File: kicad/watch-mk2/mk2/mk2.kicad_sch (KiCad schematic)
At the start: 71 parts, among them IC1 113990582, IC2 M41T62LC6F, J1 FPC24-0.5mm, J2 USB_C_Receptacle_USB2.0, J3 Conn_01x02_Female, Q1 Si1308EDL, Q2 Si1308EDL, Q3 Si1308EDL, Q4 Si1308EDL, SW1 B5, SW2 B1, SW3 B2, SW4 B3, SW5 B4, U1 W25X20CLUXIG, U2 LM3671MF-2.8_NOPB, U3 MCP73831-2-OT, Y1 32.768kHz

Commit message: add rev2mk2
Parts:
- removed C10, C11, C12, C13, C14, C15, C16, C17, C18, C19, C9: 1uF, Capacitor_SMD:C_0603_1608Metric_Pad1.05x0.95mm_HandSolder, symbol Device:C_Small
- removed C8: 4.7uF, Capacitor_SMD:C_0603_1608Metric_Pad1.05x0.95mm_HandSolder, symbol Device:C_Small
- removed D3, D4, D5: MBR0530, Diode_SMD:D_SOD-123, symbol Device:D_Schottky
- removed D6: CHRG_LED, LED_SMD:LED_0603_1608Metric_Pad1.05x0.95mm_HandSolder, symbol Device:LED
- removed D7: FLASHLIGHT, Connector_PinHeader_2.54mm:PinHeader_1x02_P2.54mm_Vertical, symbol Device:LED
- removed D8: BACKLIGHT, Connector_PinHeader_2.54mm:PinHeader_1x02_P2.54mm_Vertical, symbol Device:LED
- removed J1: FPC24-0.5mm, Connector_FFC-FPC:Hirose_FH12-24S-0.5SH_1x24-1MP_P0.50mm_Horizontal, symbol Connector:Conn_01x24_Female
- removed Q1, Q2: Si1308EDL, Package_TO_SOT_SMD:SOT-323_SC-70, symbol Device:Q_NMOS_GSD
- removed R1, R2: 1k, Resistor_SMD:R_0603_1608Metric_Pad1.05x0.95mm_HandSolder, symbol Device:R
- removed R10: 470, Resistor_SMD:R_0603_1608Metric_Pad1.05x0.95mm_HandSolder, symbol Device:R
- removed R7: 10k, Resistor_SMD:R_0603_1608Metric_Pad1.05x0.95mm_HandSolder, symbol Device:R
- removed R8: 3, Resistor_SMD:R_0603_1608Metric_Pad1.05x0.95mm_HandSolder, symbol Device:R
- removed SW3: B2, libs:E-Switch-TL3330AF130QG-MFG, symbol Switch:SW_Push
- removed SW5: B4, libs:E-Switch-TL3330AF130QG-MFG, symbol Switch:SW_Push
- removed SW_BOOT1: SW_Push, Button_Switch_SMD:SW_SPST_CK_KXT3, symbol Switch:SW_Push
- added C10: 0.47uF, Capacitor_SMD:C_0603_1608Metric_Pad1.05x0.95mm_HandSolder, symbol Device:C
- added C8: 10uF, Capacitor_SMD:C_0603_1608Metric_Pad1.05x0.95mm_HandSolder, symbol Device:C
- added C9: 560pF, Capacitor_SMD:C_0603_1608Metric_Pad1.05x0.95mm_HandSolder, symbol Device:C
- added J1: Conn_01x10_Female, Connector_FFC-FPC:Hirose_FH12-10S-0.5SH_1x10-1MP_P0.50mm_Horizontal, symbol Connector:Conn_01x10_Female
- added J5: Conn_01x04_Female, libs:ffc-0.5mm-4, symbol Connector:Conn_01x04_Female
- added JP1: FUEL_BYP, Resistor_SMD:R_0603_1608Metric, symbol Device:Jumper_NO_Small
- added P1: AXT610124, libs:PANASONIC_AXT610124, symbol AXT610124:AXT610124
- added U5: MAX17220ELT+, max17220:Maxim_Integrated-L622-1C-0-E-IPC_A, symbol max17220:MAX17220ELT+
- added U6: MAX17262REWL+T, max17262:Maxim-W91G1-3-0-A-IPC_A, symbol max17262:MAX17262REWL+T
- BT1: footprint Connector_JST:JST_PH_B2B-PH-K_1x02_P2.00mm_Vertical -> Connector_JST:JST_SH_BM02B-SRSS-TB_1x02-1MP_P1.00mm_Vertical; package (none) -> DNP
- C1, C2: LCSC (none) -> C38523; package (none) -> 0603
- C20, C4: LCSC (none) -> C19666; package (none) -> 0603
- C3, C7: LCSC (none) -> C19702; package (none) -> 0603
- C5, D2, IC2, J2, J3, SW1, SW2, SW4, SW_RESET1, TP1, TP2, TP3, TP4, U2, Y1: package (none) -> DNP
- C6: value 4.7uF -> 10uF; LCSC (none) -> C19702; package (none) -> 0603
- D1: LCSC (none) -> C155330; package (none) -> DNP
- IC1: value 113990582 -> MDBT50Q; package (none) -> DNP
- L1: package (none) -> 0603
- L2: value 10uH -> 2.2uH; package (none) -> 0603
- Q3, Q4: LCSC (none) -> C469327; package (none) -> DNP
- R11, R12: LCSC (none) -> C23186; package (none) -> 0603
- R13, R15: value 1k -> 100k; LCSC (none) -> C25803; package (none) -> 0603
- R14, R16: LCSC (none) -> C21190; package (none) -> 0603
- R3, R4: LCSC (none) -> C25190; package (none) -> 0603
- R5: value 10k -> 100k; LCSC (none) -> C25803; package (none) -> 0603
- R6: LCSC (none) -> C25804; package (none) -> 0603
- R9: LCSC (none) -> C22975; package (none) -> 0603
- U1: footprint Package_SO:TSSOP-8_4.4x3mm_P0.65mm -> libs:SON50P300X200X60-9N; LCSC (none) -> C164121; package (none) -> DNP
- U3: LCSC (none) -> C14879; package (none) -> DNP
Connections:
- net EPBUSY is gone; now on net BUTTON4: IC1.48 (P0.24)
- net EPDC is gone; now on net SCL: IC1.46 (P0.22)
- net EPSCLK is gone; now on net SDA: IC1.44 (P0.20)
- net +BATT: now also JP1.1, U6.A1 (TH), U6.A2 (BATT); no longer C20.1, D1.1 (A), U3.3 (VBAT)
- net BUTTON1: now also IC1.22 (P0.06); no longer IC1.10 (P0.29)
- net BUTTON2: now also IC1.50 (P1.02), P1.5; no longer IC1.8 (P1.15)
- net BUTTON3: now also IC1.26 (P1.09); no longer IC1.52 (P0.09/NFC1)
- net BUTTON4: now also P1.7; no longer IC1.54 (P0.10/NFC2)
- net BUTTON5: now also IC1.24 (P0.08); no longer IC1.12 (P0.31)
- net BUZZER: now also IC1.13 (P0.28); no longer IC1.6 (P1.13)
- net FLASHLIGHT: now also IC1.49 (P0.25), P1.3; no longer IC1.36 (P0.14)
- net FLASH_CS: now also IC1.16 (P0.27); no longer IC1.20 (P0.04)
- net GND: now also C6.2, TP1.1, C10.2, C8.2, C9.2, J1.10 (Pin_10), J1.9 (Pin_9), P1.9, U5.3 (GND), U5.4 (SEL), U6.C3 (GND); no longer C6.1, TP4.1
- net RTCIRQ: now also IC1.41 (P0.17); no longer IC1.14 (P0.30)
- net SCL: now also U6.B1 (SCL); no longer IC1.16 (P0.27)
- net SDA: now also U6.C1 (SDA); no longer IC1.19 (P0.26)
- net SQW: now also IC1.42 (P0.19), J1.4 (Pin_4); no longer IC1.13 (P0.28)
- net SWDIO: now also TP4.1; no longer TP1.1
- net VCC: now also R5.2, P1.2; no longer C6.2, L2.1, R5.1
- net VIN: now also C6.1, L2.1, P1.1, U5.5 (IN), U5.6 (EN)
- net VUSB: now also D1.1 (A); no longer D1.2 (A)
- net at Q3.3 (D): now also J5.3 (Pin_3), J5.4 (Pin_4)
- net at R14.2: now also J5.1 (Pin_1), J5.2 (Pin_2)
- net CHGNG: now reaches U3.1 (STAT)
- net CHGNG: now also IC1.52 (P0.09/NFC1), R5.1
- net at L2.2: now also U5.2 (LX)
- net BOOTLOAD renamed LCD_CS
- net LCD_CS: now also J1.3 (Pin_3); no longer R5.2
- net EPCS: no longer names the net of IC1.45 (P0.23)
- net EPRES: no longer names the net of IC1.47 (P1.00)
- net EPSDIN: no longer names the net of IC1.43 (P0.21)
- net FLASH_CLK renamed SPI_CLK
- net SPI_CLK: now also IC1.10 (P0.29), J1.1 (Pin_1); no longer IC1.24 (P0.08)
- net FLASH_DI renamed SPI_MOSI
- net SPI_MOSI: now also IC1.12 (P0.31), J1.2 (Pin_2); no longer IC1.26 (P1.09)
- net FLASH_DO renamed SPI_MISO
- net SPI_MISO: now also IC1.14 (P0.30); no longer IC1.22 (P0.06)
- new net: C10.1, U6.C2 (REG)
- new net 5V: C8.1, J1.6 (Pin_6), J1.7 (Pin_7), J1.8 (Pin_8), U5.1 (OUT)
- new net BATTIRQ: IC1.54 (P0.10/NFC2)
- new net BATTPOW: C20.1, D1.2 (A), JP1.2, U3.3 (VBAT), U6.B3 (SYS)
- new net LCD_DISP: C9.1, J1.5 (Pin_5)
- no-connect marks 28 -> 35
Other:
- note added: "IRQ needs pullup"
- note added: "need shunt diode to prevent cap from overcharging (??)"
- note removed: "based on https://www.waveshare.com/w/upload/8/80/E-Paper_ESP32_Driver_Board_Schematic.pdf"
- moved on the sheet: D2

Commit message: commit rev3
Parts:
- removed C5: 11mF, Capacitor_SMD:C_1210_3225Metric_Pad1.42x2.65mm_HandSolder, symbol Device:C
- removed C6: 10uF, Capacitor_SMD:C_0603_1608Metric_Pad1.05x0.95mm_HandSolder, symbol Device:C_Small
- removed C8: 10uF, Capacitor_SMD:C_0603_1608Metric_Pad1.05x0.95mm_HandSolder, symbol Device:C
- removed D2: D_Schottky, Diode_SMD:D_0603_1608Metric_Pad1.05x0.95mm_HandSolder, symbol Device:D_Schottky
- removed J5: Conn_01x04_Female, libs:ffc-0.5mm-4, symbol Connector:Conn_01x04_Female
- removed JP1: FUEL_BYP, Resistor_SMD:R_0603_1608Metric, symbol Device:Jumper_NO_Small
- removed L2: 2.2uH, Inductor_SMD:L_0603_1608Metric_Pad1.05x0.95mm_HandSolder, symbol Device:L
- removed R5: 100k, Resistor_SMD:R_0603_1608Metric_Pad1.05x0.95mm_HandSolder, symbol Device:R
- removed U1: W25X20CLUXIG, libs:SON50P300X200X60-9N, symbol Memory_Flash:AT25SF081-XMHF-X
- removed U5: MAX17220ELT+, max17220:Maxim_Integrated-L622-1C-0-E-IPC_A, symbol max17220:MAX17220ELT+
- added J4: 503480-0400, libs:MOLEX_503480-0400, symbol molex_503480-0400:503480-0400
- added U4: BMA400, libs:XDCR_BMA400, symbol BMA400:BMA400
- BT1: footprint Connector_JST:JST_SH_BM02B-SRSS-TB_1x02-1MP_P1.00mm_Vertical -> Connector_PinHeader_2.00mm:PinHeader_1x02_P2.00mm_Vertical
- J3: footprint Connector_PinHeader_1.00mm:PinHeader_1x02_P1.00mm_Vertical -> Connector_PinHeader_2.00mm:PinHeader_1x02_P2.00mm_Vertical
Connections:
- net 5V is gone; now on net VIN: J1.6 (Pin_6), J1.7 (Pin_7), J1.8 (Pin_8)
- net BACKLIGHT: now also IC1.45 (P0.23); no longer IC1.21 (P0.05)
- net GND: now also U4.1 (SDO), U4.8 (GNDIO), U4.9 (GND)
- net SCL: now also U4.12 (SCX)
- net SDA: now also U4.2 (SDX)
- net VCC: now also IC2.5 (VCC), U4.10 (~CSB~), U4.3 (VDDIO), U4.7 (VDD)
- net at R14.2: now also J4.1, J4.2
- net ACCELINT1: now reaches IC1.7 (P1.14)
- net ACCELINT1: now also U4.5 (INT1)
- net ACCELINT2: now reaches IC1.9 (P0.03)
- net ACCELINT2: now also U4.6 (INT2)
- net at Q3.3 (D): now also J4.3, J4.4
- net FLASH_CS: no longer names the net of IC1.16 (P0.27)
- no-connect marks 35 -> 36
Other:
- note removed: "IRQ needs pullup"
- note removed: "need shunt diode to prevent cap from overcharging (??)"
- moved on the sheet: J3, Q4, R15, R16

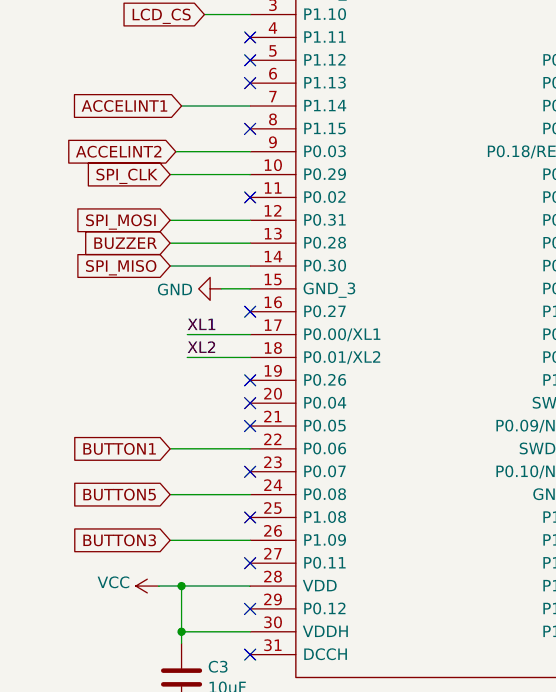
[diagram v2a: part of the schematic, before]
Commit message: add rev2 of flex cable
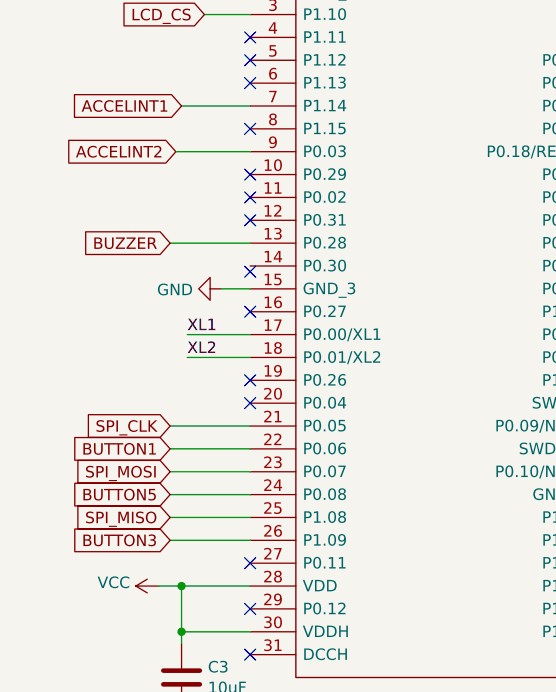
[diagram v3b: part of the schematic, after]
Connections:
- net SPI_CLK: now also IC1.21 (P0.05); no longer IC1.10 (P0.29)
- net SPI_MISO: now also IC1.25 (P1.08); no longer IC1.14 (P0.30)
- net SPI_MOSI: now also IC1.23 (P0.07); no longer IC1.12 (P0.31)
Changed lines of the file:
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@@
   (junction (at 254 147.955) (diameter 0) (color 0 0 0 0))
   (junction (at 254 155.575) (diameter 0) (color 0 0 0 0))
+  (no_connect (at 145.415 130.175))
+  (no_connect (at 38.735 144.78))
+  (no_connect (at 177.8 208.28))
+  (no_connect (at 145.415 132.715))
+  (no_connect (at 38.735 154.94))
+  (no_connect (at 38.735 132.08))
+  (no_connect (at 128.27 212.09))
+  (no_connect (at 177.8 205.74))
+  (no_connect (at 38.735 152.4))
+  (no_connect (at 125.73 212.09))
+  (no_connect (at 81.915 172.72))
+  (no_connect (at 81.915 170.18))
+  (no_connect (at 240.03 102.235))
+  (no_connect (at 81.915 144.78))
+  (no_connect (at 38.735 172.72))
+  (no_connect (at 38.735 129.54))
+  (no_connect (at 38.735 134.62))
+  (no_connect (at 38.735 140.335))
+  (no_connect (at 38.735 116.84))
+  (no_connect (at 81.915 175.26))
+  (no_connect (at 81.915 134.62))
+  (no_connect (at 81.915 124.46))
+  (no_connect (at 133.35 212.09))
+  (no_connect (at 240.03 84.455))
+  (no_connect (at 81.915 180.34))
+  (no_connect (at 81.915 121.92))
+  (no_connect (at 130.81 212.09))
+  (no_connect (at 81.915 167.64))
   (no_connect (at 81.915 116.84))
-  (no_connect (at 81.915 172.72))
-  (no_connect (at 125.73 212.09))
-  (no_connect (at 38.735 157.48))
-  (no_connect (at 38.735 162.56))
-  (no_connect (at 38.735 124.46))
-  (no_connect (at 177.8 205.74))
-  (no_connect (at 177.8 208.28))
-  (no_connect (at 81.915 134.62))
-  (no_connect (at 38.735 172.72))
-  (no_connect (at 81.915 175.26))
-  (no_connect (at 240.03 84.455))
-  (no_connect (at 38.735 154.94))
-  (no_connect (at 128.27 212.09))
-  (no_connect (at 81.915 167.64))
+  (no_connect (at 81.915 177.8))
   (no_connect (at 38.735 119.38))
-  (no_connect (at 38.735 167.64))
-  (no_connect (at 240.03 102.235))
-  (no_connect (at 38.735 132.08))
-  (no_connect (at 81.915 170.18))
-  (no_connect (at 133.35 212.09))
-  (no_connect (at 81.915 180.34))
-  (no_connect (at 81.915 124.46))
-  (no_connect (at 81.915 121.92))
-  (no_connect (at 38.735 116.84))
-  (no_connect (at 38.735 152.4))
   (no_connect (at 38.735 177.8))
-  (no_connect (at 130.81 212.09))
+  (no_connect (at 38.735 182.88))
   (no_connect (at 38.735 114.3))
   (no_connect (at 81.915 119.38))
-  (no_connect (at 81.915 177.8))
-  (no_connect (at 145.415 130.175))
-  (no_connect (at 38.735 182.88))
-  (no_connect (at 81.915 144.78))
-  (no_connect (at 145.415 132.715))
-  (no_connect (at 38.735 144.78))
+  (no_connect (at 38.735 124.46))
   (wire (pts (xy 15.24 85.09) (xy 17.78 85.09))
     (stroke (width 0) (type solid) (color 0 0 0 0))
@@
     (stroke (width 0) (type solid) (color 0 0 0 0))
   )
-  (wire (pts (xy 29.845 129.54) (xy 38.735 129.54))
-    (stroke (width 0) (type solid) (color 0 0 0 0))
-  )
-  (wire (pts (xy 29.845 134.62) (xy 38.735 134.62))
-    (stroke (width 0) (type solid) (color 0 0 0 0))
-  )
   (wire (pts (xy 29.845 137.16) (xy 38.735 137.16))
     (stroke (width 0) (type solid) (color 0 0 0 0))
   )
-  (wire (pts (xy 29.845 139.7) (xy 38.735 139.7))
+  (wire (pts (xy 29.845 157.48) (xy 38.735 157.48))
     (stroke (width 0) (type solid) (color 0 0 0 0))
   )
@@
     (stroke (width 0) (type solid) (color 0 0 0 0))
   )
+  (wire (pts (xy 29.845 162.56) (xy 38.735 162.56))
+    (stroke (width 0) (type solid) (color 0 0 0 0))
+  )
   (wire (pts (xy 29.845 165.1) (xy 38.735 165.1))
+    (stroke (width 0) (type solid) (color 0 0 0 0))
+  )
+  (wire (pts (xy 29.845 167.64) (xy 38.735 167.64))
     (stroke (width 0) (type solid) (color 0 0 0 0))
   )
@@
     (effects (font (size 1.27 1.27)) (justify left bottom))
   )
-  (global_label "SPI_CLK" (shape input) (at 29.845 129.54 180)
-    (effects (font (size 1.27 1.27)) (justify right))
-  )
-  (global_label "SPI_MOSI" (shape input) (at 29.845 134.62 180)
-    (effects (font (size 1.27 1.27)) (justify right))
-  )
   (global_label "BUZZER" (shape input) (at 29.845 137.16 180)
     (effects (font (size 1.27 1.27)) (justify right))
   )
-  (global_label "SPI_MISO" (shape input) (at 29.845 139.7 180)
+  (global_label "SPI_CLK" (shape input) (at 29.845 157.48 180)
     (effects (font (size 1.27 1.27)) (justify right))
   )
@@
     (effects (font (size 1.27 1.27)) (justify right))
   )
+  (global_label "SPI_MOSI" (shape input) (at 29.845 162.56 180)
+    (effects (font (size 1.27 1.27)) (justify right))
+  )
   (global_label "BUTTON5" (shape input) (at 29.845 165.1 180)
     (effects (font (size 1.27 1.27)) (justify right))
   )
+  (global_label "SPI_MISO" (shape input) (at 29.845 167.64 180)
+    (effects (font (size 1.27 1.27)) (justify right))
+  )

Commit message: schematic checkpoint
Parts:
- added C5, C6, C8: 2.2uF, Capacitor_SMD:C_0603_1608Metric_Pad1.05x0.95mm_HandSolder, symbol Device:C
- added J5, J6: Conn_01x02_Female, Connector_PinHeader_2.00mm:PinHeader_1x02_P2.00mm_Vertical, symbol Connector:Conn_01x02_Female
- added TP5, TP6: TestPoint, TestPoint:TestPoint_Pad_D1.0mm, symbol Connector:TestPoint
- added U1: TPS60151DRV, Package_SON:WSON-6-1EP_2x2mm_P0.65mm_EP1x1.6mm_ThermalVias, symbol Regulator_SwitchedCapacitor:TPS60151DRV
- R14: value 1k -> 100
- R16: value 1k -> 10
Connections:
- net GND: now also C5.1, C8.2, J5.2 (Pin_2), U1.1 (GND), U1.7 (EP)
- net LCD_DISP: now also IC1.4 (P1.11)
- net USB_DN: now also J6.1 (Pin_1)
- net USB_DP: now also J6.2 (Pin_2)
- net VIN: now also C5.2, TP5.1, U1.2 (VIN), U1.6 (ENA); no longer J1.6 (Pin_6), J1.7 (Pin_7), J1.8 (Pin_8)
- net VUSB: now also J5.1 (Pin_1)
- new net: C6.1, U1.4 (CP+)
- new net: C6.2, U1.5 (CP-)
- new net +5V: C8.1, J1.6 (Pin_6), J1.7 (Pin_7), J1.8 (Pin_8), TP6.1, U1.3 (VOUT)
- no-connect marks 36 -> 35
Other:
- moved on the sheet: D1

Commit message: checkpoint
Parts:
- removed J2: USB_C_Receptacle_USB2.0, Connector_USB:USB_C_Receptacle_Palconn_UTC16-G, symbol Connector:USB_C_Receptacle_USB2.0
- removed J5: Conn_01x02_Female, Connector_PinHeader_2.00mm:PinHeader_1x02_P2.00mm_Vertical, symbol Connector:Conn_01x02_Female
- removed P1: AXT610124, libs:PANASONIC_AXT610124, symbol AXT610124:AXT610124
- removed R6: 10k, Resistor_SMD:R_0603_1608Metric_Pad1.05x0.95mm_HandSolder, symbol Device:R
- removed SW_RESET1: SW_Push, Button_Switch_SMD:SW_SPST_CK_KXT3, symbol Switch:SW_Push
- added D2: D_Schottky_x2_KCom_AAK, Package_TO_SOT_SMD:TSOT-23, symbol Device:D_Schottky_x2_KCom_AAK
- added J2: 2305018-2, te-waterproof-usb-2305018-2:TE_2305018-2, symbol 2305018-2:2305018-2
- added JP1, JP2: Jumper_NO_Small, Jumper:SolderJumper-2_P1.3mm_Open_Pad1.0x1.5mm, symbol Device:Jumper_NO_Small
- added JP3: Jumper_NC_Small, Jumper:SolderJumper-2_P1.3mm_Bridged_Pad1.0x1.5mm, symbol Device:Jumper_NC_Small
- added Q1: Si1308EDL, Package_TO_SOT_SMD:SOT-323_SC-70, symbol Device:Q_NMOS_GSD
- added R1: shunt, Resistor_SMD:R_0603_1608Metric, symbol Device:R
- added R2: 100k, Resistor_SMD:R_0603_1608Metric_Pad1.05x0.95mm_HandSolder, symbol Device:R
- added U5: TPD2S017, Package_TO_SOT_SMD:SOT-23-6, symbol Power_Protection:TPD2S017
- J6: footprint Connector_PinHeader_2.00mm:PinHeader_1x02_P2.00mm_Vertical -> Connector_PinSocket_2.00mm:PinSocket_1x02_P2.00mm_Vertical; package (none) -> DNP
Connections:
- net +5V: now also D2.2 (A), JP1.2; no longer J1.6 (Pin_6), J1.7 (Pin_7), J1.8 (Pin_8)
- net FLASHLIGHT: now also Q1.1 (G), R2.1
- net GND: now also R12.1, J2.A1 (GNDA), J2.A12 (GNDA__1), J2.B1 (GNDB), J2.B12 (GNDB__1), J2.G1 (GND), J2.G2 (GND__1), J2.S1 (SHIELD), J2.S2 (SHIELD__1), J2.S3 (SHIELD__2), J2.S4 (SHIELD__3), JP2.2, Q1.2 (S), R2.2, U5.2 (GND); no longer R12.2
- net RST: now also JP2.1
- net USB_DN: now also U5.1 (CH1Out); no longer J6.1 (Pin_1)
- net USB_DP: now also U5.6 (CH2Out); no longer J6.2 (Pin_2)
- net VIN: now also J6.1 (Pin_1), D2.1 (A), JP3.1, R1.2; no longer D1.3 (K), U1.6 (ENA)
- net VUSB: now also J2.A4 (VBUS_A), J2.A9 (VBUS_A__1), J2.B4 (VBUS_B), J2.B9 (VBUS_B__1), U5.5 (VCC)
- net 5VREG_EN: now reaches IC1.16 (P0.27)
- net 5VREG_EN: now also U1.6 (ENA)
- net SPARE: now reaches IC1.37 (P0.13)
- net SIDE_INT: now reaches IC1.43 (P0.21)
- net at R11.1: now also J2.B5 (CC2)
- net BUTTON2: no longer names the net of IC1.50 (P1.02)
- net BUTTON4: no longer names the net of IC1.48 (P0.24)
- new net: J2.A5 (CC1), R12.2
- new net: D1.3 (K), JP3.2, R1.1
- new net: J6.2 (Pin_2), Q1.3 (D)
- new net DISP_POWER: D2.3 (K), J1.6 (Pin_6), J1.7 (Pin_7), J1.8 (Pin_8), JP1.1
- new net USB_DN_EXT: J2.A7 (DA_N), J2.B7 (DB_N), U5.3 (CH1In)
- new net USB_DP_EXT: J2.A6 (DA_P), J2.B6 (DB_P), U5.4 (CH2Int)
- no-connect marks 35 -> 38
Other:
- note added: "2k -> 500mA charge current (1C) 5.1k -> ~~200mA"
- note added: "RST pulled up internally"
- note removed: "2k -> 500mA charge current (1C)"
- moved on the sheet: C1, C2, C3, C5, D1, IC1, IC2, R11, R12, R3, R4, U4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

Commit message: checkpoint
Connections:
- net BATTPOW: no longer D1.2 (A)
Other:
- note added: "2k -> 500mA charge current (1C) 5.1k -> ~200mA"
- note added: "Display and Backlight"
- note added: "I/O"
- note added: "Jeff Cooper - jeff@thejeffcooper.com - Pittsburgh, PA"
- note added: "NOTE: Unclear if this 5V regulator is actually effective at such a low current level"
- note added: "Peripherals"
- note added: "Power and Battery"
- note added: "RTC"
- note added: "Sharp Memory LCD"
- note added: "Test Points"
- note added: "USB"
- note added: "accelerometer"
- note added: "https://hackaday.io/project/169967-nrf52-smartwatch"
- note added: "nRF52840"
- note added: "nRF52840 Smartwatch"
- note removed: "2k -> 500mA charge current (1C) 5.1k -> ~~200mA"
- moved on the sheet: BT1, C1, C10, C2, C20, C3, C4, C5, C6, C7, C8, C9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
